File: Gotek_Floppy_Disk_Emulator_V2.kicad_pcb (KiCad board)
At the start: 2 copper layers, 90 x 60 mm, 66 parts, among them J1 Power Connector, J2 OLED Display 0.91" Module, J3 USB_A, J5 Programming Connector, J6 Floppy Data Connector, Q1 MMBT2222, Q2 BSS123, Q3 BSS123, Q4 BSS123, Q5 BSS123, Q6 BSS123, Q7 BSS123, SW1 KY040 Rotary Encoder Module, SW2 DIP Switch, U1 AMS1117-3.3, U2 STM32F105RBTx, U3 STMPS2141, U4 74HCT04, Y1 8MHz

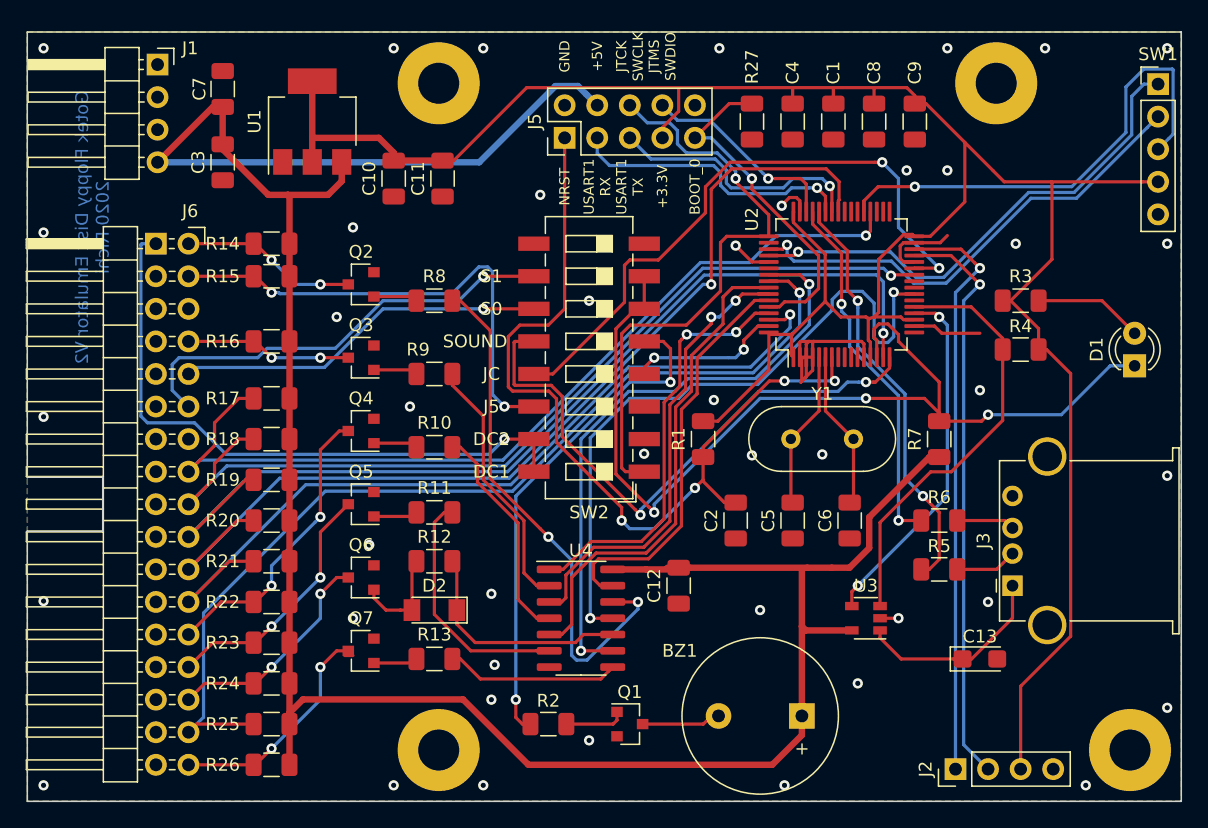
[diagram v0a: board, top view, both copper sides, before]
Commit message: Updated to KiCAD version 6
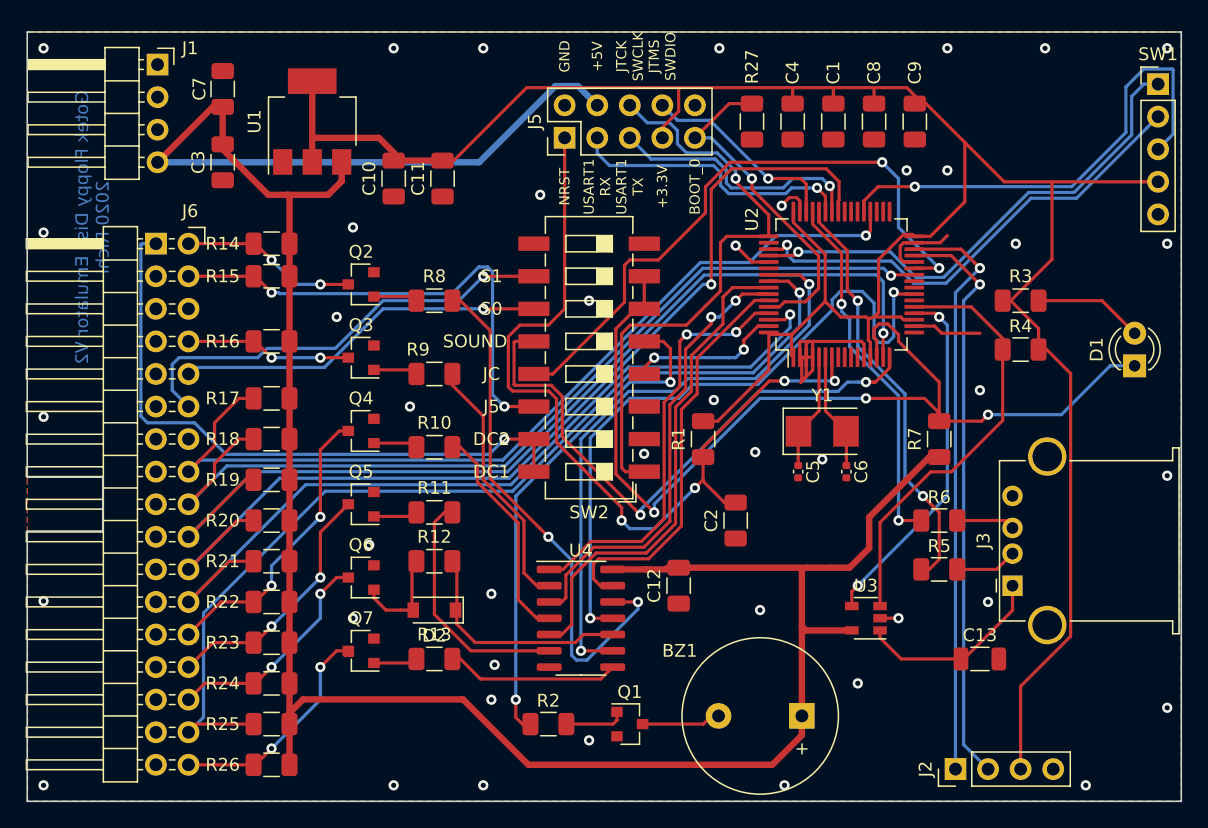
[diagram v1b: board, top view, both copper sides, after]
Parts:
- removed REF** (x4): MountingHole_3.2mm_M3_Pad, Gotek_Floppy_Disk_Emulator_V2:MountingHole_3.2mm_M3_Pad
- C13: footprint Gotek_Floppy_Disk_Emulator_V2:CP_EIA-3216-18_Kemet-A -> Capacitor_SMD:C_1206_3216Metric
- C5, C6: footprint Gotek_Floppy_Disk_Emulator_V2:C_1206_3216Metric -> Capacitor_SMD:C_0402_1005Metric
- D2: footprint Gotek_Floppy_Disk_Emulator_V2:D_MiniMELF -> Diode_SMD:D_SOD-123
- Y1: footprint Gotek_Floppy_Disk_Emulator_V2:Crystal_HC49-4H_Vertical -> Crystal:Crystal_SMD_5032-2Pin_5.0x3.2mm
- moved C5 3.83 mm to (142.0, 90.2)
- moved C6 3.82 mm to (145.8, 90.2)
- moved Y1 2.52 mm to (143.9, 87.0)
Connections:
- J1 pad 1: Net-(J1-Pad1) -> unconnected-(J1-Pad1)
- J5 pad 10: Net-(J5-Pad10) -> unconnected-(J5-Pad10)
- J6 pad 14: Net-(J6-Pad14) -> unconnected-(J6-Pad14)
- J6 pad 6: Net-(J6-Pad6) -> unconnected-(J6-Pad6)
- SW2 pad 8: Net-(SW2-Pad8) -> unconnected-(SW2-Pad8)
- SW2 pad 9: Net-(SW2-Pad9) -> unconnected-(SW2-Pad9)
- U2 pad 10: Net-(U2-Pad10) -> unconnected-(U2-Pad10)
- U2 pad 11: Net-(U2-Pad11) -> unconnected-(U2-Pad11)
- U2 pad 17: Net-(U2-Pad17) -> unconnected-(U2-Pad17)
- U2 pad 22: Net-(U2-Pad22) -> unconnected-(U2-Pad22)
- U2 pad 24: Net-(U2-Pad24) -> unconnected-(U2-Pad24)
- U2 pad 25: Net-(U2-Pad25) -> unconnected-(U2-Pad25)
- U2 pad 33: Net-(U2-Pad33) -> unconnected-(U2-Pad33)
- U2 pad 34: Net-(U2-Pad34) -> unconnected-(U2-Pad34)
- U2 pad 35: Net-(U2-Pad35) -> unconnected-(U2-Pad35)
- U2 pad 38: Net-(U2-Pad38) -> unconnected-(U2-Pad38)
- U2 pad 39: Net-(U2-Pad39) -> unconnected-(U2-Pad39)
- U2 pad 40: Net-(U2-Pad40) -> unconnected-(U2-Pad40)
- U2 pad 50: Net-(U2-Pad50) -> unconnected-(U2-Pad50)
- U2 pad 54: Net-(U2-Pad54) -> unconnected-(U2-Pad54)
- U2 pad 8: Net-(U2-Pad8) -> unconnected-(U2-Pad8)
- U2 pad 9: Net-(U2-Pad9) -> unconnected-(U2-Pad9)
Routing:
- net Net-(C6-Pad1): track 12.4 -> 9.97 mm
- net Net-(C5-Pad1): track 12.3 -> 9.97 mm
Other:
- net class Default removed
- net class Power removed
